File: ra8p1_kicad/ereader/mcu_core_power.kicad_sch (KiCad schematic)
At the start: 17 parts, among them U1 R7KA8P1KFLCAC#UC0

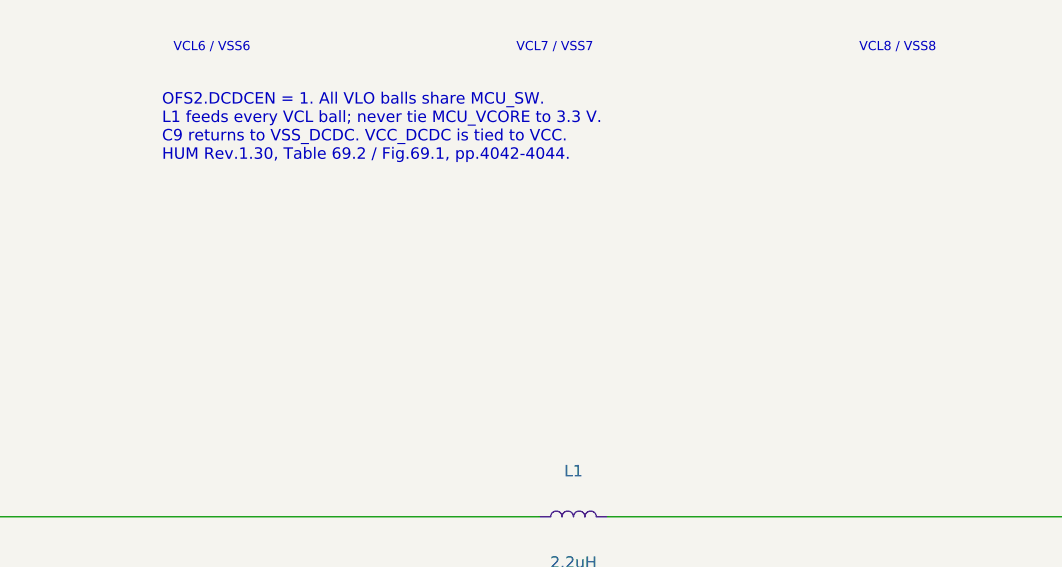
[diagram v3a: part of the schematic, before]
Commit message: Source RA8P1 core bypass capacitors with verified calculations
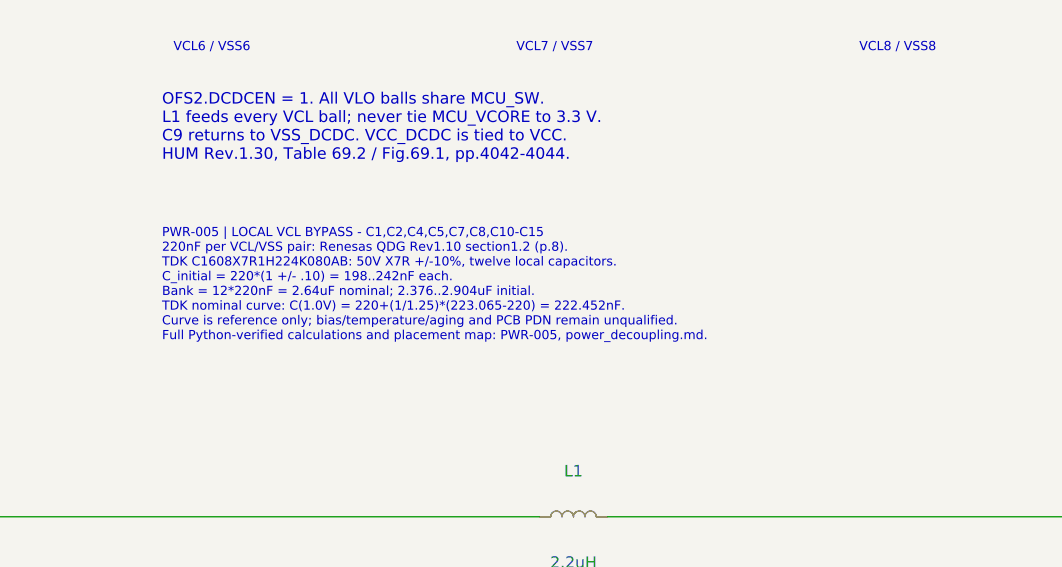
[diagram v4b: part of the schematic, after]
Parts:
- C1, C10, C11, C12, C13, C14, C15, C2, C4, C5, C7, C8: DigiKey_Part_Number (none) -> 445-7408-1-ND; DigiKey_URL (none) -> https://www.digikey.com/en/products/detail/tdk-corporation/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; Manufacturer_Name (none) -> TDK; Manufacturer_Part_Number (none) -> C1608X7R1H224K080AB; Procurement_Status TBD - exact MPN, ratings and DigiKey sourcing required -> Selected for prototype VCL bypass; PWR-005. PCB/PDN qualifi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; Selection_Basis (none) -> PWR-005: 220nF at each VCL/VSS pair per Renesas QDG Rev1.10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; Sourcing_Snapshot (none) -> 2026-09-08 DigiKey: 82010 in stock; USD0.17/0.098/0.06030 a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
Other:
- note added: "PWR-005 | LOCAL VCL BYPASS - C1,C2,C4,C5,C7,C8,C10-C15 220nF per VCL/VSS pair: Renesas QDG Rev1.10 section1.2 (p.8). TDK C1608X7R1H224K080AB: 50V X7R +/-10%, twelve local capacitors. C_initial = 220*(1 +/- .10) = 198..242nF each. Bank = 12*220nF = 2.64uF nominal; 2.376..2.904uF initial. TDK nominal curve: C(1.0V) = 220+(1/1.25)*(223.065-220) = 222.452nF. Curve is reference only; bias/temperature/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"

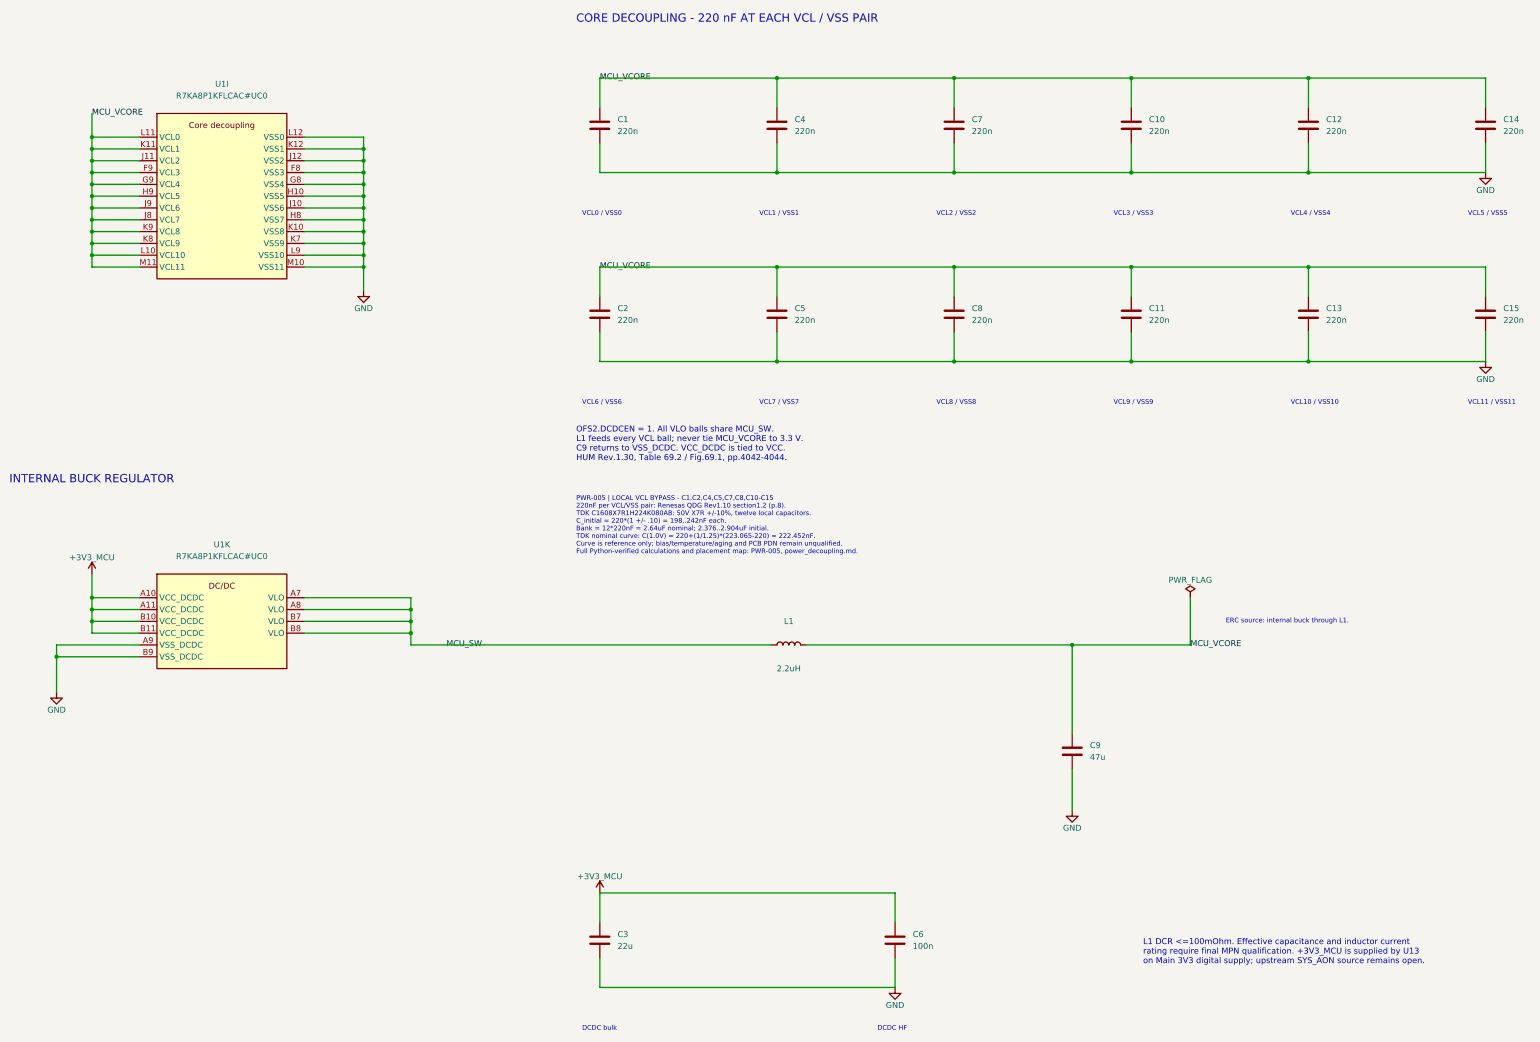
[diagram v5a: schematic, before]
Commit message: wip(hardware): preserve schematic cleanup and CEU host ports
Checkpoint cosmetic cleanup across the schematic hierarchy and eleven parallel-camera host ports. Refresh the complete 13-page PDF. All 334 existing net partitions and 271 component records match the prior CEU checkpoint; all 128 ERC identities remain unchanged. Electrical design is incomplete; this is a WIP checkpoint for #821 and #841.
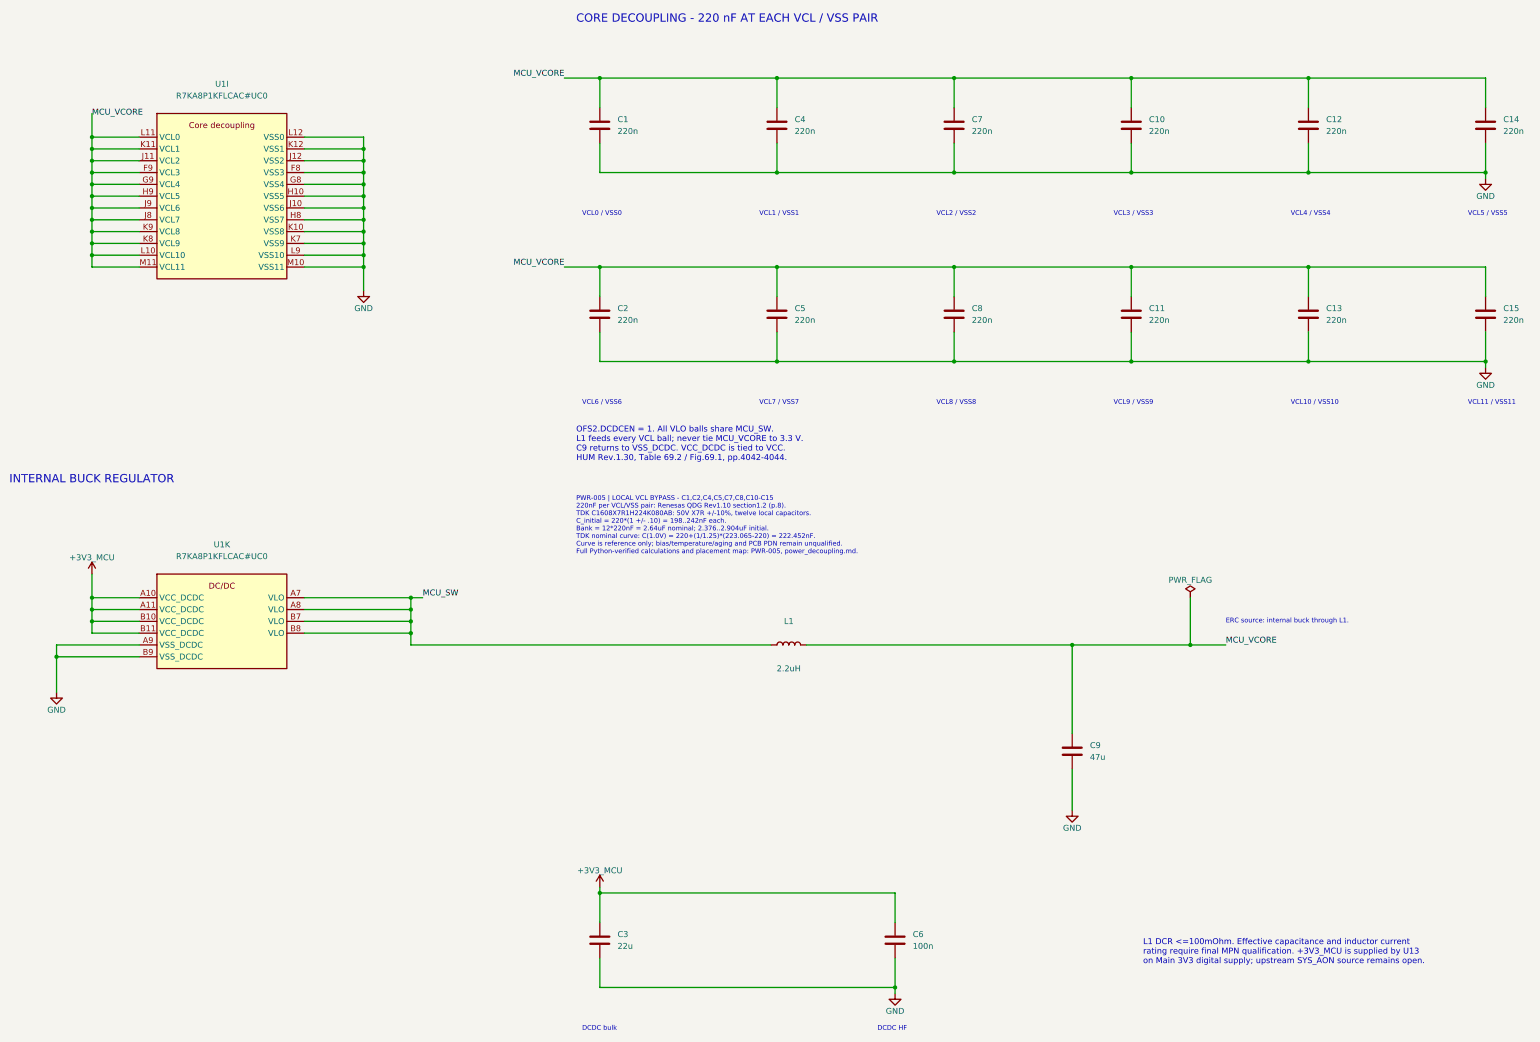
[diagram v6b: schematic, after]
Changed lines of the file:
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@@
 	)
 	(junction
+		(at 152.4 73.66)
+		(diameter 0)
+		(color 0 0 0 0)
+	)
+	(junction
 		(at 43.18 60.96)
 		(diameter 0)
@@
 	)
 	(junction
+		(at 215.9 228.6)
+		(diameter 0)
+		(color 0 0 0 0)
+	)
+	(junction
 		(at 111.76 147.32)
 		(diameter 0)
@@
 	)
 	(junction
+		(at 111.76 144.78)
+		(diameter 0)
+		(color 0 0 0 0)
+	)
+	(junction
 		(at 304.8 73.66)
 		(diameter 0)
@@
 	)
 	(junction
+		(at 152.4 33.02)
+		(diameter 0)
+		(color 0 0 0 0)
+	)
+	(junction
 		(at 266.7 73.66)
 		(diameter 0)
@@
 	)
 	(junction
+		(at 342.9 93.98)
+		(diameter 0)
+		(color 0 0 0 0)
+	)
+	(junction
 		(at 43.18 68.58)
 		(diameter 0)
@@
 	)
 	(junction
+		(at 342.9 53.34)
+		(diameter 0)
+		(color 0 0 0 0)
+	)
+	(junction
 		(at 190.5 33.02)
 		(diameter 0)
@@
 	)
 	(junction
+		(at 152.4 208.28)
+		(diameter 0)
+		(color 0 0 0 0)
+	)
+	(junction
 		(at 43.18 144.78)
 		(diameter 0)
@@
 	)
 	(junction
+		(at 279.4 154.94)
+		(diameter 0)
+		(color 0 0 0 0)
+	)
+	(junction
 		(at 43.18 71.12)
 		(diameter 0)
@@
 	(wire
 		(pts
+			(xy 111.76 144.78) (xy 114.3 144.78)
+		)
+		(stroke
+			(width 0)
+			(type default)
+		)
+	)
+	(wire
+		(pts
 			(xy 53.34 71.12) (xy 43.18 71.12)
 		)
@@
 	(wire
 		(pts
+			(xy 287.02 154.94) (xy 279.4 154.94)
+		)
+		(stroke
+			(width 0)
+			(type default)
+		)
+	)
+	(wire
+		(pts
+			(xy 144.78 73.66) (xy 152.4 73.66)
+		)
+		(stroke
+			(width 0)
+			(type default)
+		)
+	)
+	(wire
+		(pts
 			(xy 266.7 80.01) (xy 266.7 73.66)
 		)
@@
 	(wire
 		(pts
+			(xy 144.78 33.02) (xy 152.4 33.02)
+		)
+		(stroke
+			(width 0)
+			(type default)
+		)
+	)
+	(wire
+		(pts
 			(xy 101.6 50.8) (xy 101.6 53.34)
 		)
@@
 	(wire
 		(pts
+			(xy 215.9 222.25) (xy 215.9 229.87)
+		)
+		(stroke
+			(width 0)
+			(type default)
+		)
+	)
+	(wire
+		(pts
 			(xy 101.6 63.5) (xy 101.6 66.04)
 		)
@@
 	(wire
 		(pts
-			(xy 342.9 87.63) (xy 342.9 93.98)
-		)
-		(stroke
-			(width 0)
-			(type default)
-		)
-	)
-	(wire
-		(pts
 			(xy 43.18 63.5) (xy 43.18 66.04)
 		)
@@
 	(wire
 		(pts
-			(xy 152.4 214.63) (xy 152.4 208.28)
+			(xy 152.4 207.01) (xy 152.4 214.63)
 		)
 		(stroke
@@
 	(wire
 		(pts
-			(xy 342.9 46.99) (xy 342.9 53.34)
+			(xy 342.9 46.99) (xy 342.9 54.61)
 		)
 		(stroke
@@
 	(wire
 		(pts
-			(xy 215.9 222.25) (xy 215.9 228.6)
+			(xy 53.34 50.8) (xy 43.18 50.8)
 		)
 		(stroke
@@
 	(wire
 		(pts
-			(xy 53.34 50.8) (xy 43.18 50.8)
+			(xy 190.5 80.01) (xy 190.5 73.66)
 		)
 		(stroke
@@
 	(wire
 		(pts
-			(xy 190.5 80.01) (xy 190.5 73.66)
+			(xy 152.4 33.02) (xy 152.4 39.37)
 		)
 		(stroke
@@
 	(wire
 		(pts
-			(xy 53.34 144.78) (xy 43.18 144.78)
+			(xy 342.9 87.63) (xy 342.9 95.25)
 		)
 		(stroke
@@
 	(wire
 		(pts
-			(xy 43.18 139.7) (xy 43.18 144.78)
+			(xy 53.34 144.78) (xy 43.18 144.78)
 		)
 		(stroke
@@
 	(wire
 		(pts
-			(xy 43.18 60.96) (xy 43.18 63.5)
+			(xy 43.18 139.7) (xy 43.18 144.78)
 		)
 		(stroke
@@
 	(wire
 		(pts
-			(xy 152.4 39.37) (xy 152.4 33.02)
+			(xy 43.18 60.96) (xy 43.18 63.5)
 		)
 		(stroke
@@
 	)
 	(label "MCU_VCORE"
-		(at 279.4 154.94 0)
+		(at 287.02 154.94 0)
 		(effects
 			(font
 				(size 1.27 1.27)
 			)
+			(justify left bottom)
 		)
 	)
 	(label "MCU_VCORE"
-		(at 152.4 33.02 0)
+		(at 144.78 73.66 180)
 		(effects
 			(font
 				(size 1.27 1.27)
 			)
+			(justify right bottom)
 		)
 	)
-	(label "MCU_SW"
-		(at 119.38 154.94 0)
+	(label "MCU_VCORE"
+		(at 43.18 40.64 0)
 		(effects
 			(font
@@
 	)
 	(label "MCU_VCORE"
-		(at 152.4 73.66 0)
+		(at 144.78 33.02 180)
 		(effects
 			(font
 				(size 1.27 1.27)
 			)
+			(justify right bottom)
 		)
 	)
-	(label "MCU_VCORE"
-		(at 43.18 40.64 0)
+	(label "MCU_SW"
+		(at 114.3 144.78 0)
 		(effects
 			(font
 				(size 1.27 1.27)
 			)
+			(justify left bottom)
 		)
 	)
@@
 	(symbol
 		(lib_id "power:GND")
-		(at 215.9 228.6 0)
+		(at 215.9 229.87 0)
 		(unit 1)
 		(body_style 1)
@@
 		(dnp no)
 		(property "Reference" "#PWR05"
-			(at 215.9 234.95 0)
+			(at 215.9 236.22 0)
 			(hide yes)
 			(show_name no)
@@
 		)
 		(property "Value" "GND"
-			(at 215.9 232.41 0)
+			(at 215.9 233.68 0)
 			(show_name no)
 			(do_not_autoplace no)
@@
 		)
 		(property "Footprint" ""
-			(at 215.9 228.6 0)
+			(at 215.9 229.87 0)
 			(hide yes)
 			(show_name no)
@@
 		)
 		(property "Datasheet" ""
-			(at 215.9 228.6 0)
+			(at 215.9 229.87 0)
 			(hide yes)
 			(show_name no)
@@
 		)
 		(property "Description" "Power symbol creates a global label with name \"GND\" , ground"
-			(at 215.9 228.6 0)
+			(at 215.9 229.87 0)
 			(hide yes)
 			(show_name no)
@@
 		)
 		(property "ki_keywords" "global power"
-			(at 215.9 228.6 0)
+			(at 215.9 229.87 0)
 			(hide yes)
 			(show_name no)
@@
 	(symbol
 		(lib_id "power:+3V3")
-		(at 152.4 208.28 0)
+		(at 152.4 207.01 0)
 		(unit 1)
 		(body_style 1)
@@
 		(dnp no)
 		(property "Reference" "#PWR04"
-			(at 152.4 212.09 0)
+			(at 152.4 210.82 0)
 			(hide yes)
 			(show_name no)
@@
 		)
 		(property "Value" "+3V3_MCU"
-			(at 152.4 204.724 0)
+			(at 152.4 203.454 0)
 			(show_name no)
 			(do_not_autoplace no)
@@
 		)
 		(property "Footprint" ""
-			(at 152.4 208.28 0)
+			(at 152.4 207.01 0)
 			(hide yes)
 			(show_name no)
@@
 		)
 		(property "Datasheet" ""
-			(at 152.4 208.28 0)
+			(at 152.4 207.01 0)
 			(hide yes)
 			(show_name no)
@@
 		)
 		(property "Description" "Power symbol creates a global label with name \"+3V3\""
-			(at 152.4 208.28 0)
+			(at 152.4 207.01 0)
 			(hide yes)
 			(show_name no)
@@
 		)
 		(property "ki_keywords" "global power"
-			(at 152.4 208.28 0)
+			(at 152.4 207.01 0)
 			(hide yes)
 			(show_name no)
@@
 	(symbol
 		(lib_id "power:GND")
-		(at 342.9 93.98 0)
+		(at 342.9 95.25 0)
 		(unit 1)
 		(body_style 1)
@@
 		(dnp no)
 		(property "Reference" "#PWR08"
-			(at 342.9 100.33 0)
+			(at 342.9 101.6 0)
 			(hide yes)
 			(show_name no)
@@
 		)
 		(property "Value" "GND"
-			(at 342.9 97.79 0)
+			(at 342.9 99.06 0)
 			(show_name no)
 			(do_not_autoplace no)
@@
 		)
 		(property "Footprint" ""
-			(at 342.9 93.98 0)
+			(at 342.9 95.25 0)
 			(hide yes)
 			(show_name no)
@@
 		)
 		(property "Datasheet" ""
-			(at 342.9 93.98 0)
+			(at 342.9 95.25 0)
 			(hide yes)
 			(show_name no)
@@
 		)
 		(property "Description" "Power symbol creates a global label with name \"GND\" , ground"
-			(at 342.9 93.98 0)
+			(at 342.9 95.25 0)
 			(hide yes)
 			(show_name no)
@@
 		)
 		(property "ki_keywords" "global power"
-			(at 342.9 93.98 0)
+			(at 342.9 95.25 0)
 			(hide yes)
 			(show_name no)
@@
 	(symbol
 		(lib_id "power:GND")
-		(at 342.9 53.34 0)
+		(at 342.9 54.61 0)
 		(unit 1)
 		(body_style 1)
@@
 		(dnp no)
 		(property "Reference" "#PWR07"
-			(at 342.9 59.69 0)
+			(at 342.9 60.96 0)
 			(hide yes)
 			(show_name no)
@@
 		)
 		(property "Value" "GND"
-			(at 342.9 57.15 0)
+			(at 342.9 58.42 0)
 			(show_name no)
 			(do_not_autoplace no)
@@
 		)
 		(property "Footprint" ""
-			(at 342.9 53.34 0)
+			(at 342.9 54.61 0)
 			(hide yes)
 			(show_name no)
@@
 		)
 		(property "Datasheet" ""
-			(at 342.9 53.34 0)
+			(at 342.9 54.61 0)
 			(hide yes)
 			(show_name no)
@@
 		)
 		(property "Description" "Power symbol creates a global label with name \"GND\" , ground"
-			(at 342.9 53.34 0)
+			(at 342.9 54.61 0)
 			(hide yes)
 			(show_name no)
@@
 		)
 		(property "ki_keywords" "global power"
-			(at 342.9 53.34 0)
+			(at 342.9 54.61 0)
 			(hide yes)
 			(show_name no)
